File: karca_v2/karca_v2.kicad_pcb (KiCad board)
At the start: 4 copper layers, 250 x 145 mm, 361 parts, among them J1 CON_FAN1, J10 Keyhole ignition switch, J11 Screw_Terminal_01x04, J12 Buzzer, J2 Conn_Batt, J3 USB_B_Micro, J4 LoadCell_1_2, J5 LoadCell_3_4, J6 Screw_Terminal_01x08, J7 Raspberry_pi, J8 Screw_Terminal_01x08, J9 Screw_Terminal_01x10, Q1 AO3401A, Q10 IRF3708, Q11 IRF3708, Q12 IRF3708, Q13 IRF3708, Q2 PN2222A, Q4 IRF3708, Q9 IRF3708, SW1 SW_SPST, SW2 SW_SPST, SW3 SW_SPST, U1 TVS1400DRV, U10 NUP4202, U11 M41T93, U12 NUP4202, U13 TLV9304xD, U14 TS5A3159ADBVR, U17 TS5A3159ADBVR, U19 TS5A3159ADBVR, U2 MCP3208, U22 TS5A3159ADBVR, U24 AD8495, U26 AD8495, U27 AD8495, U29 AD8495, U3 NUP4202, U30 INA180A4, U32 NUP4202, U33 AD8223, U34 INA180A2, U35 AD8223, U36 TLV9301xDBV, U4 TLV9304xD, U41 NUP4202, U42 MCP3204, U43 AD8223, U44 AD8223, U5 TLV9304xD, U6 TPS7A24, U7 TLV9304xD, U8 TLV9304xD, U9 MCP3208

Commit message: quick fix
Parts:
- U10: renamed from U12; footprint Package_SO:TSOP-6_1.65x3.05mm_P0.95mm -> Package_TO_SOT_SMD:SOT-363_SC-70-6
- U3, U32, U41: footprint Package_SO:TSOP-6_1.65x3.05mm_P0.95mm -> Package_TO_SOT_SMD:SOT-363_SC-70-6
- moved C5 147.0 mm to (190.4, 146.2)
- moved U9 147.0 mm to (187.2, 141.1)
- moved TP57 146.5 mm to (199.2, 132.7)
- moved TP56 141.9 mm to (195.2, 132.6)
- moved U12 141.2 mm to (184.3, 126.1)
- moved TP12 141.2 mm to (185.3, 134.1)
- moved TP19 140.6 mm to (171.8, 133.8)
- moved TP13 140.6 mm to (181.1, 132.6)
- moved TP21 139.2 mm to (168.8, 131.3)
- moved TP58 138.0 mm to (188.8, 130.2)
- moved TP55 134.8 mm to (191.3, 132.5)
- moved TP10 134.2 mm to (179.7, 129.7)
- moved U32 133.0 mm to (191.6, 126.9)
- moved TP11 131.4 mm to (179.3, 138.0)
- moved TP17 130.5 mm to (161.8, 129.7)
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- renumbered U10 to U12
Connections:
- C52 pad 2: /Drivers/DRV1_ADC -> /DRV1_ADC
- C54 pad 2: /Drivers/DRV2_ADC -> /DRV2_ADC
- C55 pad 2: /Drivers/DRV3_ADC -> /DRV3_ADC
- C57 pad 2: /Drivers/DRV4_ADC -> /DRV4_ADC
- Ce1 pad 1: /Pressure Transducers/TC_1_ADC -> /Load Cells/TC_1_ADC
- Ce2 pad 1: /Pressure Transducers/TC_2_ADC -> /Load Cells/TC_2_ADC
- Ce3 pad 1: /Pressure Transducers/TC_3_ADC -> /Load Cells/TC_3_ADC
- Ce4 pad 1: /Pressure Transducers/TC_4_ADC -> /Load Cells/TC_4_ADC
- D4 pad 2: +5V -> Net-(D4-A)
- J3 pad 1: +5V -> Net-(D4-A)
- J7 pad 29: Net-(J7-Pin_29) -> unconnected-(J7-Pin_29-Pad29)
- J7 pad 3: unconnected-(J7-Pin_3-Pad3) -> Net-(J7-Pin_3)
- Q1 pad 1: +5V -> Net-(D4-A)
- R10 pad 2: Net-(J7-Pin_29) -> Net-(J7-Pin_3)
- R101 pad 2: /Drivers/DRV2_ADC -> /DRV2_ADC
- R103 pad 2: /Drivers/DRV3_ADC -> /DRV3_ADC
- R105 pad 2: /Drivers/DRV4_ADC -> /DRV4_ADC
- R11 pad 2: Net-(J7-Pin_29) -> Net-(J7-Pin_3)
- R99 pad 2: /Drivers/DRV1_ADC -> /DRV1_ADC
- TP14 pad 1: /Pressure Transducers/TC_1_ADC -> /Load Cells/TC_1_ADC
- TP15 pad 1: /Pressure Transducers/TC_1_ADC -> /Load Cells/TC_1_ADC
- TP16 pad 1: /Pressure Transducers/TC_2_ADC -> /Load Cells/TC_2_ADC
- TP17 pad 1: /Pressure Transducers/TC_2_ADC -> /Load Cells/TC_2_ADC
- TP18 pad 1: /Pressure Transducers/TC_3_ADC -> /Load Cells/TC_3_ADC
- TP19 pad 1: /Pressure Transducers/TC_3_ADC -> /Load Cells/TC_3_ADC
- TP20 pad 1: /Pressure Transducers/TC_4_ADC -> /Load Cells/TC_4_ADC
- TP21 pad 1: /Pressure Transducers/TC_4_ADC -> /Load Cells/TC_4_ADC
- TP5 pad 1: +5V -> Net-(D4-A)
- TP55 pad 1: /Drivers/DRV1_ADC -> /DRV1_ADC
- TP56 pad 1: /Drivers/DRV2_ADC -> /DRV2_ADC
- TP57 pad 1: /Drivers/DRV3_ADC -> /DRV3_ADC
- TP58 pad 1: /Drivers/DRV4_ADC -> /DRV4_ADC
- U10 pad 1: /Pressure Transducers/TC_4_ADC -> /Load Cells/TC_1_ADC
- U10 pad 3: /Pressure Transducers/TC_3_ADC -> /Load Cells/TC_2_ADC
- U10 pad 4: /Pressure Transducers/TC_2_ADC -> /Load Cells/TC_3_ADC
- U10 pad 6: /Pressure Transducers/TC_1_ADC -> /Load Cells/TC_4_ADC
- U12 pad 1: /Pressure Transducers/pt_circuitry3/OUT -> /Pressure Transducers/pt_circuitry/OUT
- U12 pad 3: /Pressure Transducers/pt_circuitry2/OUT -> /Pressure Transducers/pt_circuitry1/OUT
- U12 pad 4: /Pressure Transducers/pt_circuitry1/OUT -> /Pressure Transducers/pt_circuitry2/OUT
- U12 pad 6: /Pressure Transducers/pt_circuitry/OUT -> /Pressure Transducers/pt_circuitry3/OUT
- U13 pad 1: /Pressure Transducers/TC_2_ADC -> /Load Cells/TC_2_ADC
- U13 pad 13: /Pressure Transducers/TC_3_ADC -> /Load Cells/TC_3_ADC
- U13 pad 14: /Pressure Transducers/TC_3_ADC -> /Load Cells/TC_3_ADC
- U13 pad 2: /Pressure Transducers/TC_2_ADC -> /Load Cells/TC_2_ADC
- U13 pad 6: /Pressure Transducers/TC_1_ADC -> /Load Cells/TC_1_ADC
- U13 pad 7: /Pressure Transducers/TC_1_ADC -> /Load Cells/TC_1_ADC
- U13 pad 8: /Pressure Transducers/TC_4_ADC -> /Load Cells/TC_4_ADC
- U13 pad 9: /Pressure Transducers/TC_4_ADC -> /Load Cells/TC_4_ADC
- U2 pad 1: /Load Cells/LC_Amplification/OUT -> /Load Cells/TC_3_ADC
- U2 pad 2: /Load Cells/LC_Amplification1/OUT -> /Load Cells/TC_4_ADC
- U2 pad 3: /Load Cells/LC_Amplification2/OUT -> /Load Cells/TC_1_ADC
- U2 pad 4: /Load Cells/LC_Amplification3/OUT -> /Load Cells/TC_2_ADC
- U2 pad 5: /Drivers/DRV1_ADC -> /Load Cells/LC_Amplification/OUT
- U2 pad 6: /Drivers/DRV2_ADC -> /Load Cells/LC_Amplification1/OUT
- U2 pad 7: /Drivers/DRV3_ADC -> /Load Cells/LC_Amplification2/OUT
- U2 pad 8: /Drivers/DRV4_ADC -> /Load Cells/LC_Amplification3/OUT
- U3 pad 4: /Load Cells/LC_Amplification1/OUT -> /Load Cells/LC_Amplification/OUT
- U3 pad 6: /Load Cells/LC_Amplification/OUT -> /Load Cells/LC_Amplification1/OUT
- U32 pad 1: /Drivers/DRV1_ADC -> /DRV3_ADC
- U32 pad 3: /Drivers/DRV4_ADC -> /DRV2_ADC
- U32 pad 4: /Drivers/DRV3_ADC -> /DRV1_ADC
- U32 pad 6: /Drivers/DRV2_ADC -> /DRV4_ADC
- U9 pad 1: /Pressure Transducers/pt_circuitry/OUT -> /DRV3_ADC
- U9 pad 2: /Pressure Transducers/pt_circuitry1/OUT -> /DRV2_ADC
- U9 pad 3: /Pressure Transducers/pt_circuitry2/OUT -> /DRV1_ADC
- U9 pad 4: /Pressure Transducers/pt_circuitry3/OUT -> /DRV4_ADC
- U9 pad 5: /Pressure Transducers/TC_1_ADC -> /Pressure Transducers/pt_circuitry2/OUT
- U9 pad 6: /Pressure Transducers/TC_2_ADC -> /Pressure Transducers/pt_circuitry3/OUT
- U9 pad 7: /Pressure Transducers/TC_3_ADC -> /Pressure Transducers/pt_circuitry/OUT
- U9 pad 8: /Pressure Transducers/TC_4_ADC -> /Pressure Transducers/pt_circuitry1/OUT
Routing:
- net /Pressure Transducers/TC_3_ADC: track 257.3 -> 0.00 mm, vias 2 -> 0
- net /Drivers/DRV4_ADC: track 238.4 -> 0.00 mm, vias 2 -> 0
- net /Drivers/DRV2_ADC: track 233.4 -> 0.00 mm, vias 2 -> 0
- net /Drivers/DRV3_ADC: track 227.3 -> 0.00 mm, vias 2 -> 0
- net /Pressure Transducers/TC_2_ADC: track 221.0 -> 0.00 mm, vias 2 -> 0
- net /Pressure Transducers/TC_4_ADC: track 219.6 -> 0.00 mm, vias 2 -> 0
- net /Pressure Transducers/TC_1_ADC: track 201.4 -> 0.00 mm, vias 2 -> 0
- net /Load Cells/LC_SELECTOR: track 0.00 -> 194.8 mm, vias 0 -> 4
- net /Drivers/IGN_CONT: track 253.9 -> 134.1 mm, vias 1 -> 2
- net /Drivers/DRV4_CTL: track 186.4 -> 72.4 mm, vias 1 -> 0
- net /Drivers/DRV5_CTL: track 180.1 -> 70.9 mm, vias 1 -> 0
- net /Drivers/DRV2_CTL: track 197.1 -> 88.6 mm, vias 1 -> 0
- net /Drivers/DRV3_CTL: track 179.3 -> 74.0 mm, vias 1 -> 0
- net /Drivers/DRV1_CTL: track 205.3 -> 100.4 mm, vias 1 -> 0
- net /Load Cells/TC_2_ADC: track 0.00 -> 97.3 mm
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- added copper zone on F.Cu, net +12V

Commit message: Checkpoint before ripping everything apart
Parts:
- moved C3 59.6 mm to (171.4, 50.0)
- moved C4 59.6 mm to (172.9, 58.1)
- moved R6 59.6 mm to (174.9, 50.9)
- moved R7 59.6 mm to (175.1, 47.1)
- moved U6 59.6 mm to (174.6, 54.9)
- moved R10 14.4 mm to (144.0, 165.0), turned to 0 degrees
- moved D6 12.0 mm to (144.5, 179.1), turned to 180 degrees
- moved Q2 11.2 mm to (142.5, 174.4), turned to 0 degrees
- moved R11 11.1 mm to (144.0, 168.3), turned to 0 degrees
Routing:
- net Net-(J7-Pin_3): track 9.40 -> 12.7 mm

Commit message: Saved the 12V rail
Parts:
- moved R9 154.4 mm to (33.9, 168.2), turned to 90 degrees
- moved C6 149.5 mm to (33.9, 173.8), turned to 90 degrees
- moved U11 146.3 mm to (41.2, 168.5), turned to 0 degrees
- moved R8 138.1 mm to (48.7, 169.0), turned to -90 degrees
- moved R10 110.3 mm to (35.4, 145.8)
- moved D6 110.3 mm to (35.9, 159.9)
- moved Q2 110.3 mm to (34.0, 155.2)
- moved R11 110.3 mm to (35.4, 149.1)
- moved J7 98.7 mm to (54.3, 145.8), turned to 0 degrees
- moved C1 70.3 mm to (132.7, 170.5)
- moved C72 70.3 mm to (121.5, 173.2)
- moved D3 70.3 mm to (116.6, 173.4)
- moved D4 70.3 mm to (141.8, 180.9)
- moved D5 70.3 mm to (121.3, 182.4)
- moved MD1 70.3 mm to (124.5, 164.4)
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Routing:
- net /Drivers/DRV3_CTL: track 74.0 -> 200.5 mm, vias 0 -> 1
- net /Drivers/IGN_CONT: track 134.1 -> 256.4 mm
- net /SPI.MISO: track 136.2 -> 252.9 mm, vias 2 -> 0
- net /Drivers/DRV5_CTL: track 70.9 -> 186.5 mm, vias 0 -> 1
- net /Drivers/DRV4_CTL: track 72.4 -> 185.1 mm, vias 0 -> 1
- net /Load Cells/LC_SELECTOR: track 194.8 -> 86.1 mm
- net /Drivers/DRV2_CTL: track 88.6 -> 197.0 mm
- net /SPI.MOSI: track 143.4 -> 251.6 mm
- net /Drivers/DRV1_CTL: track 100.4 -> 202.7 mm, vias 0 -> 1
- net /Pressure Transducers/CS: track 34.2 -> 136.4 mm
- net Net-(U42-CH0): track 115.0 -> 27.7 mm, vias 2 -> 1
- net /Load Cells/LC_CS: track 34.8 -> 108.9 mm
- net Net-(U36--): track 90.3 -> 21.5 mm, vias 2 -> 1
- net Net-(U44-REF): track 8.64 -> 59.6 mm, vias 0 -> 2
- net Net-(U44-OUT): track 8.08 -> 56.7 mm
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
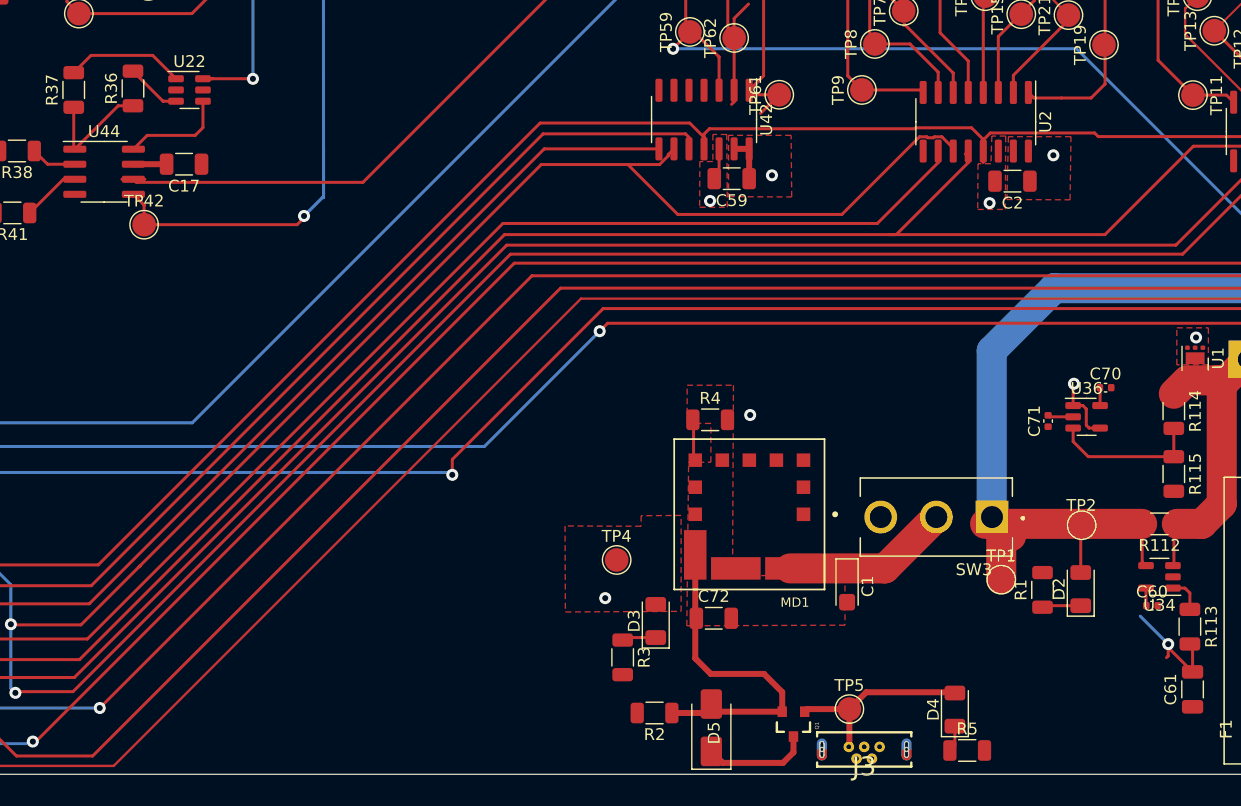
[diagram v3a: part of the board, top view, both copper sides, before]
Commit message: rearrange regs
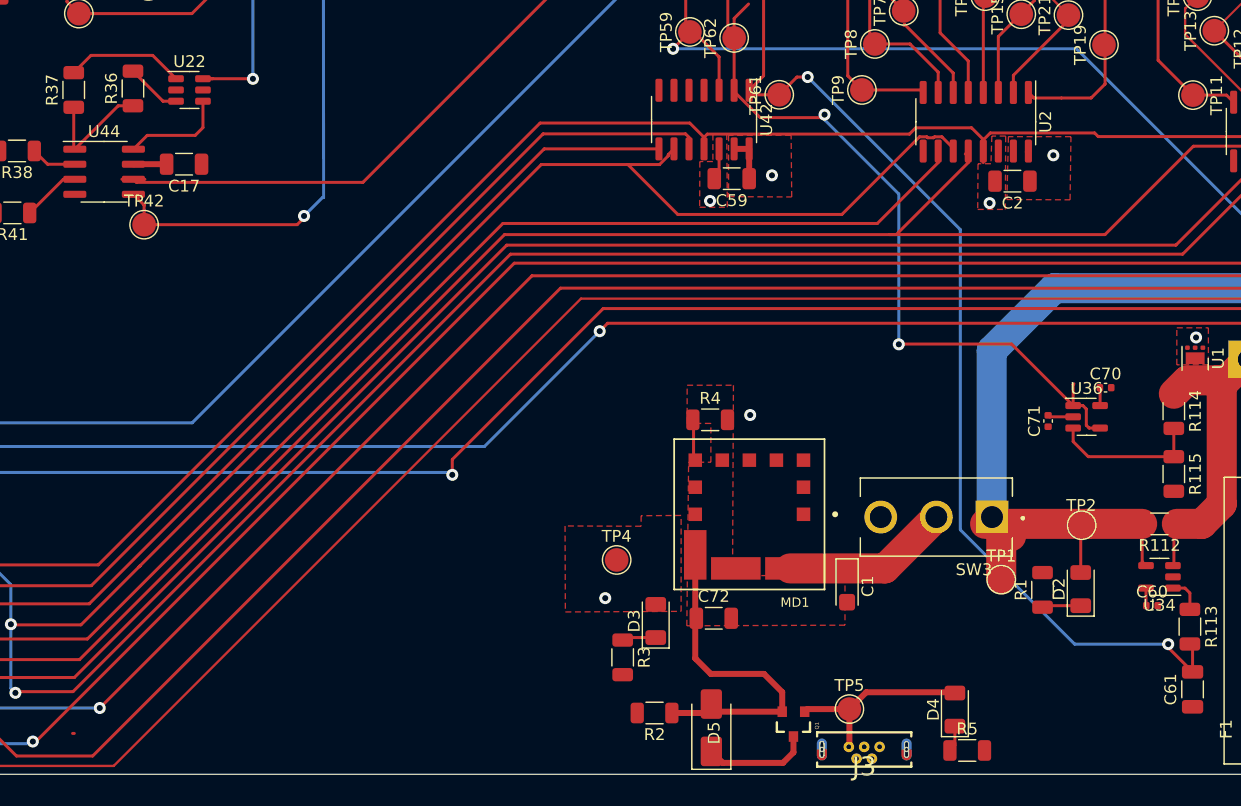
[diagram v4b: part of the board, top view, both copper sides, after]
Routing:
- net Net-(U42-CH0): track 27.7 -> 89.2 mm, vias 1 -> 2
- net Net-(U36--): track 21.5 -> 68.2 mm, vias 1 -> 2
- net /SPI.CLK: track 141.6 -> 140.5 mm
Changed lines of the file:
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@@
   (segment (start 60.815853 174.613719) (end 60.4774 174.952172) (width 0.254) (layer "B.Cu") (net 66))
   (segment (start 56.2544 165.7924) (end 60.815853 170.353853) (width 0.254) (layer "B.Cu") (net 66))
+  (segment (start 143.257599 131.7711) (end 138.540654 131.7711) (width 0.254) (layer "F.Cu") (net 67))
   (segment (start 69.4814 168.6944) (end 55.1564 168.6944) (width 0.254) (layer "F.Cu") (net 67))
   (segment (start 144.2466 132.7983) (end 144.2466 133.7351) (width 0.254) (layer "F.Cu") (net 67))
   (segment (start 55.1564 168.6944) (end 54.2544 167.7924) (width 0.254) (layer "F.Cu") (net 67))
-  (segment (start 138.460353 131.8514) (end 121.1072 131.8514) (width 0.254) (layer "F.Cu") (net 67))
   (segment (start 120.6571 132.575201) (end 119.450699 131.3688) (width 0.254) (layer "F.Cu") (net 67))
   (segment (start 45.881399 172.3136) (end 46.906398 172.3136) (width 0.254) (layer "F.Cu") (net 67))
   (segment (start 153.6517 132.207) (end 144.8379 132.207) (width 0.254) (layer "F.Cu") (net 67))
-  (segment (start 121.1072 131.8514) (end 120.6571 132.3015) (width 0.254) (layer "F.Cu") (net 67))
   (segment (start 106.807 131.3688) (end 69.4814 168.6944) (width 0.254) (layer "F.Cu") (net 67))
-  (segment (start 144.2466 132.760101) (end 143.257599 131.7711) (width 0.254) (layer "F.Cu") (net 67))
+  (segment (start 138.010254 132.3015) (end 120.930801 132.3015) (width 0.254) (layer "F.Cu") (net 67))
   (segment (start 119.450699 131.3688) (end 106.807 131.3688) (width 0.254) (layer "F.Cu") (net 67))
+  (segment (start 144.2466 133.7351) (end 144.2466 132.760101) (width 0.254) (layer "F.Cu") (net 67))
   (segment (start 144.8379 132.207) (end 144.2466 132.7983) (width 0.254) (layer "F.Cu") (net 67))
   (segment (start 170.4736 132.7333) (end 170.2521 132.5118) (width 0.254) (layer "F.Cu") (net 67))
-  (segment (start 138.540654 131.7711) (end 138.460353 131.8514) (width 0.254) (layer "F.Cu") (net 67))
-  (segment (start 144.2466 133.7351) (end 144.2466 132.760101) (width 0.254) (layer "F.Cu") (net 67))
-  (segment (start 120.6571 132.3015) (end 120.6571 133.5502) (width 0.254) (layer "F.Cu") (net 67))
+  (segment (start 144.2466 132.760101) (end 143.257599 131.7711) (width 0.254) (layer "F.Cu") (net 67))
+  (segment (start 120.6571 132.575201) (end 120.6571 133.5502) (width 0.254) (layer "F.Cu") (net 67))
   (segment (start 170.4736 134.5591) (end 170.4736 132.7333) (width 0.254) (layer "F.Cu") (net 67))
   (segment (start 170.2521 132.5118) (end 153.9565 132.5118) (width 0.254) (layer "F.Cu") (net 67))
   (segment (start 144.2466 134.710099) (end 144.2466 133.7351) (width 0.254) (layer "F.Cu") (net 67))
-  (segment (start 143.257599 131.7711) (end 138.540654 131.7711) (width 0.254) (layer "F.Cu") (net 67))
-  (segment (start 120.6571 133.5502) (end 120.6571 132.575201) (width 0.254) (layer "F.Cu") (net 67))
+  (segment (start 138.540654 131.7711) (end 138.010254 132.3015) (width 0.254) (layer "F.Cu") (net 67))
+  (segment (start 120.930801 132.3015) (end 120.6571 132.575201) (width 0.254) (layer "F.Cu") (net 67))
   (segment (start 153.9565 132.5118) (end 153.6517 132.207) (width 0.254) (layer "F.Cu") (net 67))
   (segment (start 68.72157 171.9834) (end 60.061847 171.9834) (width 0.254) (layer "F.Cu") (net 68))
@@
   (segment (start 108.5342 145.3134) (end 69.0118 184.8358) (width 0.254) (layer "F.Cu") (net 74))
   (segment (start 200.6011 145.3134) (end 108.5342 145.3134) (width 0.254) (layer "F.Cu") (net 74))
+  (segment (start 67.31 182.9308) (end 67.4624 182.9308) (width 0.254) (layer "F.Cu") (net 75))
   (segment (start 193.2627 144.272) (end 106.1212 144.272) (width 0.254) (layer "F.Cu") (net 75))
   (segment (start 224.8849 112.6498) (end 193.2627 144.272) (width 0.254) (layer "F.Cu") (net 75))
@@
   (segment (start 206.244 75.5792) (end 206.244 76.8492) (width 0.2) (layer "F.Cu") (net 164))
   (segment (start 220.4822 101.727) (end 220.4822 84.582) (width 0.2) (layer "F.Cu") (net 164))
-  (segment (start 159.7152 176.53) (end 159.8676 176.3776) (width 0.254) (layer "F.Cu") (net 165))
   (segment (start 125.6863 120.6246) (end 124.4265 119.3648) (width 0.254) (layer "F.Cu") (net 165))
   (segment (start 125.6863 127.381) (end 125.6863 120.6246) (width 0.254) (layer "F.Cu") (net 165))
   (segment (start 124.4265 119.3648) (end 122.7647 119.3648) (width 0.254) (layer "F.Cu") (net 165))
-  (segment (start 159.8676 176.3776) (end 159.8676 175.387) (width 0.254) (layer "F.Cu") (net 165))
   (segment (start 122.7647 119.3648) (end 122.3871 118.9872) (width 0.254) (layer "F.Cu") (net 165))
   (segment (start 161.924983 175.6007) (end 161.698683 175.3744) (width 0.254) (layer "F.Cu") (net 165))
@@
   (segment (start 159.8676 175.674017) (end 159.8676 175.387) (width 0.254) (layer "F.Cu") (net 165))
   (segment (start 124.8481 128.9812) (end 127.0081 128.9812) (width 0.254) (layer "F.Cu") (net 165))
-  (segment (start 127.0081 128.9812) (end 125.4333 130.556) (width 0.254) (layer "F.Cu") (net 165))
+  (segment (start 129.413 127.4826) (end 129.286 127.4826) (width 0.254) (layer "F.Cu") (net 165))
   (segment (start 161.924983 177.7314) (end 161.924983 175.6007) (width 0.254) (layer "F.Cu") (net 165))
+  (segment (start 128.5067 127.4826) (end 129.413 127.4826) (width 0.254) (layer "F.Cu") (net 165))
   (segment (start 124.4671 128.6002) (end 124.8481 128.9812) (width 0.254) (layer "F.Cu") (net 165))
+  (segment (start 127.0081 128.9812) (end 128.5067 127.4826) (width 0.254) (layer "F.Cu") (net 165))
+  (via (at 129.413 127.4826) (size 1.016) (drill 0.508) (layers "F.Cu" "B.Cu") (net 165))
   (via (at 159.8676 175.387) (size 1.016) (drill 0.508) (layers "F.Cu" "B.Cu") (net 165))
-  (segment (start 159.8676 175.387) (end 157.500845 173.020245) (width 0.254) (layer "B.Cu") (net 165))
+  (segment (start 142.303883 165.722683) (end 151.9682 175.387) (width 0.254) (layer "B.Cu") (net 165))
+  (segment (start 151.9682 175.387) (end 159.8676 175.387) (width 0.254) (layer "B.Cu") (net 165))
+  (segment (start 142.303883 140.373483) (end 142.303883 165.722683) (width 0.254) (layer "B.Cu") (net 165))
+  (segment (start 129.413 127.4826) (end 142.303883 140.373483) (width 0.254) (layer "B.Cu") (net 165))
   (segment (start 123.1971 124.1806) (end 122.6637 123.6472) (width 0.254) (layer "F.Cu") (net 166))
   (segment (start 152.948 155.5258) (end 152.948 156.8974) (width 0.254) (layer "F.Cu") (net 166))
+  (segment (start 151.835883 155.2349) (end 146.638783 150.0378) (width 0.254) (layer "F.Cu") (net 166))
   (segment (start 152.948 156.8974) (end 153.1855 157.1349) (width 0.254) (layer "F.Cu") (net 166))
   (segment (start 151.835883 155.2349) (end 152.6571 155.2349) (width 0.254) (layer "F.Cu") (net 166))
+  (segment (start 123.1971 128.704686) (end 123.1971 128.6002) (width 0.254) (layer "F.Cu") (net 166))
   (segment (start 120.7839 118.8972) (end 120.4871 118.8972) (width 0.254) (layer "F.Cu") (net 166))
+  (segment (start 137.1092 150.0632) (end 137.1346 150.0378) (width 0.254) (layer "F.Cu") (net 166))
   (segment (start 153.1855 157.1349) (end 154.110883 157.1349) (width 0.254) (layer "F.Cu") (net 166))
+  (segment (start 146.638783 150.0378) (end 137.1854 150.0378) (width 0.254) (layer "F.Cu") (net 166))
   (segment (start 123.1971 124.1806) (end 123.1971 128.6002) (width 0.254) (layer "F.Cu") (net 166))
-  (segment (start 123.1971 129.575199) (end 122.978299 129.794) (width 0.254) (layer "F.Cu") (net 166))
+  (segment (start 137.1854 150.0378) (end 137.1092 150.0632) (width 0.254) (layer "F.Cu") (net 166))
   (segment (start 122.6637 123.6472) (end 122.6637 120.777) (width 0.254) (layer "F.Cu") (net 166))
+  (segment (start 137.1346 150.0378) (end 137.16 150.0378) (width 0.254) (layer "F.Cu") (net 166))
   (segment (start 151.835883 155.2349) (end 151.835883 153.458917) (width 0.254) (layer "F.Cu") (net 166))
   (segment (start 123.1971 122.5312) (end 124.4163 121.312) (width 0.254) (layer "F.Cu") (net 166))
-  (segment (start 123.1971 128.6002) (end 123.1971 129.575199) (width 0.254) (layer "F.Cu") (net 166))
   (segment (start 122.6637 120.777) (end 120.7839 118.8972) (width 0.254) (layer "F.Cu") (net 166))
+  (segment (start 130.8354 130.6576) (end 130.5814 130.9116) (width 0.254) (layer "F.Cu") (net 166))
+  (segment (start 130.5814 130.9116) (end 125.404014 130.9116) (width 0.254) (layer "F.Cu") (net 166))
   (segment (start 152.6571 155.2349) (end 152.948 155.5258) (width 0.254) (layer "F.Cu") (net 166))
+  (segment (start 125.404014 130.9116) (end 123.1971 128.704686) (width 0.254) (layer "F.Cu") (net 166))
   (segment (start 120.5555 118.9656) (end 120.4871 118.8972) (width 0.254) (layer "F.Cu") (net 166))
   (segment (start 151.835883 153.458917) (end 151.9036 153.3912) (width 0.254) (layer "F.Cu") (net 166))
   (segment (start 123.1971 124.1806) (end 123.1971 122.5312) (width 0.254) (layer "F.Cu") (net 166))
-  (via (at 151.9036 153.3912) (size 1.016) (drill 0.508) (layers "F.Cu" "B.Cu") (net 166))
+  (via (at 130.8354 130.6576) (size 1.016) (drill 0.508) (layers "F.Cu" "B.Cu") (net 166))
+  (via (at 137.1092 150.0632) (size 1.016) (drill 0.508) (layers "F.Cu" "B.Cu") (net 166))
+  (segment (start 137.1092 137.3632) (end 130.8862 131.1402) (width 0.254) (layer "B.Cu") (net 166))
+  (segment (start 137.1092 143.3068) (end 137.1092 137.3632) (width 0.254) (layer "B.Cu") (net 166))
+  (segment (start 130.8354 130.6576) (end 130.7084 130.7846) (width 0.254) (layer "B.Cu") (net 166))
+  (segment (start 130.7084 130.9624) (end 130.8354 130.6576) (width 0.254) (layer "B.Cu") (net 166))
+  (segment (start 137.1092 150.0632) (end 137.1092 143.3068) (width 0.254) (layer "B.Cu") (net 166))
+  (segment (start 130.8862 131.1402) (end 130.7084 130.9624) (width 0.254) (layer "B.Cu") (net 166))
   (segment (start 151.835883 158.274483) (end 153.1137 159.5523) (width 0.254) (layer "F.Cu") (net 167))
   (segment (start 153.1137 159.5523) (end 160.339383 159.5523) (width 0.254) (layer "F.Cu") (net 167))
